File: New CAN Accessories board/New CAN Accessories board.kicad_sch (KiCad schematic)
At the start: 0 parts

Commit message: updated schematic to add high side sensing, haven't speced specific components yet
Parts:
- added C1, C2: 100nF, Capacitor_SMD:C_0805_2012Metric, symbol Device:C
- added D1, D2, D3, D4, D5, D6, D7, D9: LED, LED_SMD:LED_0805_2012Metric, symbol Device:LED
- added F1, F2, F3, F4, F5, F6, F7, F9: Fuse, FuseClips:3586KTR, symbol Device:Fuse
- added J1, J2, J3, J4, J5, J6, J7, J8: 39301040, Connector_Molex:Molex_Mini-Fit_Jr_5569-04A2_2x02_P4.20mm_Horizontal, symbol Connector_Generic:Conn_02x02_Top_Bottom
- added J10, J9: 39301060, Connector_Molex:Molex_Mini-Fit_Jr_5569-06A2_2x03_P4.20mm_Horizontal, symbol Connector_Generic:Conn_02x03_Top_Bottom
- added JP4: SolderJumper_2_Open, Jumper:SolderJumper-2_P1.3mm_Open_Pad1.0x1.5mm, symbol Jumper:SolderJumper_2_Open
- added Q1, Q2, Q3, Q4, Q5, Q6, Q7, Q8: IRF7455PBFTR, Package_SO:SOIC-8-1EP_3.9x4.9mm_P1.27mm_EP2.29x3mm, symbol Device:Q_NMOS_SGD
- added R1, R11, R13, R3, R42, R5, R7, R9: 100, Resistor_SMD:R_0805_2012Metric, symbol Device:R
- added R10, R12, R14, R2, R4, R43, R6, R8: 10K, Resistor_SMD:R_0805_2012Metric, symbol Device:R
- added R13: 120, Resistor_SMD:R_0805_2012Metric, symbol Device:R
- added R15, R16, R17, R18, R19, R20, R21, R22, R23, R24, R25, R26, R27, R28, R29, R30, R31, R32, R33, R34, R35, R36, R37, R38, R39, R40, R41, R44, R45, R46, R47, R48, R49, R50, R51, R52, R53, R54, R55, R56: R, symbol Device:R
- added U1: NUCLEO_L432KC, NUCLEO-L432KC:MODULE_NUCLEO-L432KC, symbol CAN_Accessories-rescue:NUCLEO_L432KC-NUCLEO-L432KC
- added U10, U3, U4, U5, U6, U7, U8, U9: OPA1662DGK, Package_SO:VSSOP-8_3x3mm_P0.65mm, symbol Amplifier_Operational:OPA1662DGK
- added U2: MCP2562FD-E_SN, MCP2562FD-E_SN:MCP2562FD-E_SN, symbol CAN_Accessories-rescue:MCP2562FD-E_SN-2021-02-19_16-08-03
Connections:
- new net: J1.1 (Pin_1), J1.2 (Pin_2), R17.2, R19.1
- new net: F1.1, J1.3 (Pin_3), J1.4 (Pin_4)
- new net: J2.1 (Pin_1), J2.2 (Pin_2), R22.2, R24.1
- new net: F2.1, J2.3 (Pin_3), J2.4 (Pin_4)
- new net: J3.1 (Pin_1), J3.2 (Pin_2), R27.2, R29.1
- new net: F3.1, J3.3 (Pin_3), J3.4 (Pin_4)
- new net: J4.1 (Pin_1), J4.2 (Pin_2), R32.2, R34.1
- new net: F4.1, J4.3 (Pin_3), J4.4 (Pin_4)
- new net: J5.1 (Pin_1), J5.2 (Pin_2), R36.2, R38.1
- new net: F5.1, J5.3 (Pin_3), J5.4 (Pin_4)
- new net: J7.1 (Pin_1), J7.2 (Pin_2), R48.2, R50.1
- new net: F6.1, J7.3 (Pin_3), J7.4 (Pin_4)
- new net: JP4.1 (A), R13.2
- new net: F1.2, Q1.3 (D)
- new net: D1.2 (A), R1.2
- new net: D5.2 (A), R9.2
- new net: R33.2, R35.1, U6.3 (+)
- new net: R23.2, R25.1, U4.3 (+)
- new net: R34.2, R40.1, U6.2 (-)
- new net: R50.2, R55.1, U9.2 (-)
- new net: R19.2, R20.1, U3.2 (-)
- new net: F7.1, J8.3 (Pin_3), J8.4 (Pin_4)
- new net: F7.2, Q8.3 (D)
- new net: R38.2, R41.1, U7.2 (-)
- new net: J6.2 (Pin_2), R44.2, R46.1
- new net: F4.2, Q4.3 (D)
- new net: J8.1 (Pin_1), J8.2 (Pin_2), R15.2, R52.1
- new net: R52.2, R56.1, U10.2 (-)
- new net: D2.2 (A), R3.2
- new net: R24.2, R26.1, U4.2 (-)
- new net: F9.1, J6.3 (Pin_3), J6.4 (Pin_4)
- new net: F9.2, Q6.3 (D)
- new net: R49.2, R51.1, U9.3 (+)
- new net: F6.2, Q7.3 (D)
- new net: R16.2, R53.1, U10.3 (+)
- new net: D7.2 (A), R13.2
- new net: F5.2, Q5.3 (D)
- new net: R45.2, R47.1, U8.3 (+)
- new net: F3.2, Q3.3 (D)
- new net: R46.2, R54.1, U8.2 (-)
- new net: R29.2, R31.1, U5.2 (-)
- new net: D9.2 (A), R42.2
- new net: D3.2 (A), R5.2
- new net: R37.2, R39.1, U7.3 (+)
- new net: R18.2, R21.1, U3.3 (+)
- new net: R28.2, R30.1, U5.3 (+)
- new net: D6.2 (A), R11.2
- new net: F2.2, Q2.3 (D)
- new net: D4.2 (A), R7.2
- new net +12V: J10.1 (Pin_1), J10.2 (Pin_2), J9.1 (Pin_1), J9.2 (Pin_2), R15.1, R16.1, R17.1, R18.1, R22.1, R23.1, R27.1, R28.1, R32.1, R33.1, R36.1, R37.1, R44.1, R45.1, R48.1, R49.1, U1.VIN
- new net 3V3: C2.1, U2.5 (VIO)
- new net 5V: C1.1, U1.5V, U2.3 (VDD)
- new net CANH: J10.5 (Pin_5), J9.5 (Pin_5), R13.1, U2.7 (CANH)
- new net CANL: J10.4 (Pin_4), J9.4 (Pin_4), JP4.2 (B), U2.6 (CANL)
- new net CANRX: U1.PA11 (D10), U2.4 (RXD)
- new net CANTX: U1.PA12 (D2), U2.1 (TXD)
- new net GATE1: Q1.2 (G), R1.1, R2.1, U1.PA2 (A7)
- new net GATE2: Q2.2 (G), R3.1, R4.1, U1.PA7 (A6)
- new net GATE3: Q3.2 (G), R5.1, R6.1, U1.PB7 (D4)
- new net GATE4: Q4.2 (G), R7.1, R8.1, U1.PB6 (D5)
- new net GATE5: Q5.2 (G), R10.1, R9.1, U1.PB5 (D11)
- new net GATE6: Q6.2 (G), Q7.2 (G), R11.1, R12.1, R42.1, R43.1, U1.PB4 (D12)
- new net GATE7: Q8.2 (G), R13.1, R14.1
- new net GND: C1.2, C2.2, D1.1 (K), D2.1 (K), D3.1 (K), D4.1 (K), D5.1 (K), D6.1 (K), D7.1 (K), D9.1 (K), J10.3 (Pin_3), J10.6 (Pin_6), J9.3 (Pin_3), J9.6 (Pin_6), Q1.1 (S), Q2.1 (S), Q3.1 (S), Q4.1 (S), Q5.1 (S), Q6.1 (S), Q7.1 (S), Q8.1 (S), R10.2, R12.2, R14.2, R2.2, R20.2, R26.2, R31.2, R4.2, R40.2, R41.2, R43.2, R54.2, R55.2, R56.2, R6.2, R8.2, U1.GND, U2.2 (VSS)
- new net OA1: R21.2, U1.PA0 (A0), U3.1
- new net OA2: R25.2, U1.PA1 (A1), U4.1
- new net OA3: R30.2, U1.PA3 (A2), U5.1
- new net OA4: R35.2, U1.PA4 (A3), U6.1
- new net OA5: R39.2, U1.PA5 (A4), U7.1
- new net OA6: R47.2, U1.PA6 (A5), U8.1
- new net OA7: R51.2, U1.PA8 (D9), U9.1
- new net OA8: R53.2, U1.PB1 (D6), U10.1
- new net STBY: U1.PA9 (D1), U2.8 (STBY)
- no-connect marks 0 -> 9

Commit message: updated kicad schematic to include new op amps and update layout
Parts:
- removed D4, D5, D6, D9: LED, LED_SMD:LED_0805_2012Metric, symbol Device:LED
- removed J4, J5, J6: 39301040, Connector_Molex:Molex_Mini-Fit_Jr_5569-04A2_2x02_P4.20mm_Horizontal, symbol Connector_Generic:Conn_02x02_Top_Bottom
- removed R10, R12, R14, R43: 10K, Resistor_SMD:R_0805_2012Metric, symbol Device:R
- removed R11, R42, R9: 100, Resistor_SMD:R_0805_2012Metric, symbol Device:R
- removed R15, R16, R21, R22, R25, R26, R27, R28, R29, R30, R31, R32, R33, R34, R35, R36, R37, R38, R39, R40, R41, R44, R45, R46, R47, R48, R49, R50, R51, R52, R53, R54, R55, R56: R, symbol Device:R
- removed U10, U3, U4, U5, U6, U7, U8, U9: OPA1662DGK, Package_SO:VSSOP-8_3x3mm_P0.65mm, symbol Amplifier_Operational:OPA1662DGK
- added D4 (x2), D5 (x2), D6 (x2), D8: LED, LED_SMD:LED_0805_2012Metric, symbol Device:LED
- added F10, F11, F8: Fuse, FuseClips:3586KTR, symbol Device:Fuse
- added J4 (x2), J5 (x2), J6 (x2): 39301040, Connector_Molex:Molex_Mini-Fit_Jr_5569-04A2_2x02_P4.20mm_Horizontal, symbol Connector_Generic:Conn_02x02_Top_Bottom
- added OP1, OP2, OP3, OP4, OP5, OP6, OP7, OP8, U6, U7, U8: MCP6C02T-020E/CHY, SOT-23-6_CHY_MCH, symbol sym:MCP6C02T-020E_CHY
- added Q10, Q11, Q9: IRF7455PBFTR, Package_SO:SOIC-8-1EP_3.9x4.9mm_P1.27mm_EP2.29x3mm, symbol Device:Q_NMOS_SGD
- added R10 (x2), R12, R14 (x2), R16, R21: 10K, Resistor_SMD:R_0805_2012Metric, symbol Device:R
- added R11, R12, R15, R16, R9 (x2): 100, Resistor_SMD:R_0805_2012Metric, symbol Device:R
- added R11, R15, R21, R22 (x2): 0.05, symbol Device:R
- added R57: 10K, symbol Device:R
- added SW1: SW_SPST, symbol Switch:SW_SPST
- R17, R18, R19, R20, R23, R24: value R -> 0.05
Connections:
- net GATE7 is gone; now on net GATE1: Q8.2 (G), R13.1
- net +12V: now also R19.1, R20.1, R24.1, OP1.3 (VIP), OP2.3 (VIP), OP3.3 (VIP), OP4.3 (VIP), OP5.3 (VIP), OP6.3 (VIP), OP7.3 (VIP), OP8.3 (VIP), R11.1, R15.1, R21.1, R22.1, R22.1, U6.3 (VIP), U7.3 (VIP), U8.3 (VIP)
- net 5V: now also OP1.6 (VDD), OP2.6 (VDD), OP3.6 (VDD), OP4.6 (VDD), OP5.6 (VDD), OP6.6 (VDD), OP7.6 (VDD), OP8.6 (VDD), U6.6 (VDD), U7.6 (VDD), U8.6 (VDD)
- net GATE1: now also Q2.2 (G), Q3.2 (G), Q4.2 (G), Q5.2 (G), Q6.2 (G), Q7.2 (G), R3.1, R4.1, R5.1, R6.1, R7.1, R8.1, U1.PB1 (D6), Q10.2 (G), Q11.2 (G), Q9.2 (G), R10.1, R10.1, R11.1, R12.1, R12.1, R14.1, R14.1, R15.1, R16.1, R16.1, R21.1, R9.1, R9.1; no longer U1.PA2 (A7)
- net GATE2: now also U1.PA8 (D9); no longer Q2.2 (G), R3.1, R4.1, U1.PA7 (A6)
- net GATE3: no longer Q3.2 (G), R5.1, R6.1
- net GATE4: no longer Q4.2 (G), R7.1, R8.1
- net GATE5: no longer Q5.2 (G)
- net GATE6: no longer Q6.2 (G), Q7.2 (G)
- net GND: now also D4.1 (K), D5.1 (K), D6.1 (K), D8.1 (K), OP1.2 (VSS), OP1.5 (VREF), OP2.2 (VSS), OP2.5 (VREF), OP3.2 (VSS), OP3.5 (VREF), OP4.2 (VSS), OP4.5 (VREF), OP5.2 (VSS), OP5.5 (VREF), OP6.2 (VSS), OP6.5 (VREF), OP7.2 (VSS), OP7.5 (VREF), OP8.2 (VSS), OP8.5 (VREF), Q10.1 (S), Q11.1 (S), Q9.1 (S), R10.2, R12.2, R14.2, R16.2, R57.2, U6.2 (VSS), U7.2 (VSS), U8.2 (VSS); no longer Q4.1 (S), Q5.1 (S), Q6.1 (S), R20.2
- net OA1: now also OP1.1 (VOUT), U6.1 (VOUT), U7.1 (VOUT), U8.1 (VOUT)
- net OA2: now also OP2.1 (VOUT)
- net OA3: now also OP3.1 (VOUT)
- net OA4: now also OP4.1 (VOUT)
- net OA5: now also OP5.1 (VOUT)
- net OA6: now also OP6.1 (VOUT)
- net OA7: now also U1.PA7 (A6), OP7.1 (VOUT); no longer U1.PA8 (D9)
- net OA8: now also U1.PA2 (A7), OP8.1 (VOUT); no longer U1.PB1 (D6)
- net at J1.1 (Pin_1), J1.2 (Pin_2), R17.2: now also OP1.4 (VIM); no longer R19.1
- net at J2.1 (Pin_1), J2.2 (Pin_2): now also R18.2, OP2.4 (VIM); no longer R24.1
- net at J2.3 (Pin_3), J2.4 (Pin_4): now also F8.1; no longer F2.1
- net at J3.1 (Pin_1), J3.2 (Pin_2): now also R19.2, OP3.4 (VIM)
- net at J3.3 (Pin_3), J3.4 (Pin_4): now also F2.1; no longer F3.1
- net at F4.1: now also J4.3 (Pin_3), J4.4 (Pin_4)
- net at F5.1: now also J5.3 (Pin_3), J5.4 (Pin_4)
- net at J7.1 (Pin_1), J7.2 (Pin_2): now also R23.2, OP7.4 (VIM)
- net at J7.3 (Pin_3), J7.4 (Pin_4): now also F10.1; no longer F6.1
- net at U1.3V3: now also SW1.1 (A)
- net at U1.PB3 (D13): now also R57.1, SW1.2 (B)
- net at J8.3 (Pin_3), J8.4 (Pin_4): now also F11.1; no longer F7.1
- net at Q8.3 (D): now also F9.2; no longer F7.2
- net at J8.1 (Pin_1), J8.2 (Pin_2): now also R24.2, OP8.4 (VIM)
- net at F9.1: now also J6.3 (Pin_3), J6.4 (Pin_4)
- net at Q6.3 (D): now also F6.2; no longer F9.2
- net at Q7.3 (D): now also F7.2; no longer F6.2
- net at R7.2: now also D4.2 (A)
- new net: J4.1 (Pin_1), J4.2 (Pin_2), R11.2, U6.4 (VIM)
- new net: D4.1 (K), Q4.1 (S), R10.2, U6.5 (VREF)
- new net: J6.1 (Pin_1), J6.2 (Pin_2), OP6.4 (VIM), R22.2
- new net: J4.1 (Pin_1), J4.2 (Pin_2), OP4.4 (VIM), R20.2
- new net: F6.1, J6.3 (Pin_3), J6.4 (Pin_4)
- new net: J6.1 (Pin_1), J6.2 (Pin_2), R22.2, U8.4 (VIM)
- new net: D6.1 (K), Q6.1 (S), R21.2, U8.5 (VREF)
- new net: J5.1 (Pin_1), J5.2 (Pin_2), OP5.4 (VIM), R21.2
- new net: D4.2 (A), R9.2
- new net: D6.2 (A), R11.2
- new net: D5.1 (K), Q5.1 (S), R14.2, U7.5 (VREF)
- new net: F3.1, J4.3 (Pin_3), J4.4 (Pin_4)
- new net: D5.2 (A), R12.2
- new net: F11.2, Q11.3 (D)
- new net: F10.2, Q10.3 (D)
- new net: F8.2, Q9.3 (D)
- new net: F7.1, J5.3 (Pin_3), J5.4 (Pin_4)
- new net: D8.2 (A), R15.2
- new net: J5.1 (Pin_1), J5.2 (Pin_2), R15.2, U7.4 (VIM)
- new net: D6.2 (A), R16.2
- new net: D5.2 (A), R9.2
- no-connect marks 9 -> 7
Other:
- moved on the sheet: C1, C2, D1, F1, J1, J10, J9, JP4, Q1, R1, R13, R17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

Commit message: updated schematic again, all parts match bom, for final review
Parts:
- removed Q1, Q10, Q11, Q2, Q3, Q7, Q8, Q9: IRF7455PBFTR, Package_SO:SOIC-8-1EP_3.9x4.9mm_P1.27mm_EP2.29x3mm, symbol Device:Q_NMOS_SGD
- removed SW1: SW_SPST, symbol Switch:SW_SPST
- added Q1, Q2, Q4, Q5, Q6, Q7, Q8: IRLML6344TRPBF, IRLML6344TRPBF:TRANS_IRLML6344TRPBF, symbol sym:IRLML6344TRPBF
- added R27: 10K, symbol Device:R
- added SW1, SW2: JS202011CQN, SWITCH_011CQN, symbol sym:JS202011CQN
- renumbered F8 to F2, F2 to F3, F3 to F4, F7 to F5, F9 to F6, F10 to F7, R13 to R25, R57 to R26
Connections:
- net 3V3: now also SW1.1, SW1.2, SW1.3, SW2.1, SW2.2, SW2.3
- net GATE1: now also Q1.1; no longer R10.1, R11.1, R12.1, R13.1, R14.1, R15.1, R16.1, R3.1, R4.1, R5.1, R6.1, R7.1, R8.1, R9.1
- net GATE2: now also R3.1, R4.1, Q2.1
- net GATE3: now also R5.1, R6.1, Q1.1
- net GATE4: now also R7.1, R8.1, Q4.1
- net GATE5: now also R10.1, R9.1, Q5.1
- net GATE6: now also R11.1, R12.1, Q6.1
- net GND: now also Q1.2, Q2.2, Q4.2, Q5.2, Q6.2, Q7.2, Q8.2, R27.2
- net at F1.2: now also Q1.3
- net BOARD_SW: now reaches U1.PB0 (D3)
- net BOARD_SW: now also R27.1, SW2.4, SW2.5, SW2.6
- net TELEM_SW: now reaches R26.1, U1.PB3 (D13)
- net TELEM_SW: now also SW1.4, SW1.5, SW1.6
- net at F6.2: now also Q6.3
- net at F4.2: now also Q4.3
- net at F11.2: now also Q8.3
- net at F7.2: now also Q7.3
- net at F3.2: now also Q1.3
- net at F2.2: now also Q2.3
- net at F5.2: now also Q5.3
- new net GATE7: Q7.1, R13.1, R14.1
- new net GATE8: Q8.1, R15.1, R16.1
- no-connect marks 7 -> 6
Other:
- moved on the sheet: C1, C2, F1, F11, F2, F3, F4, F5, F6, F7, J10, J9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

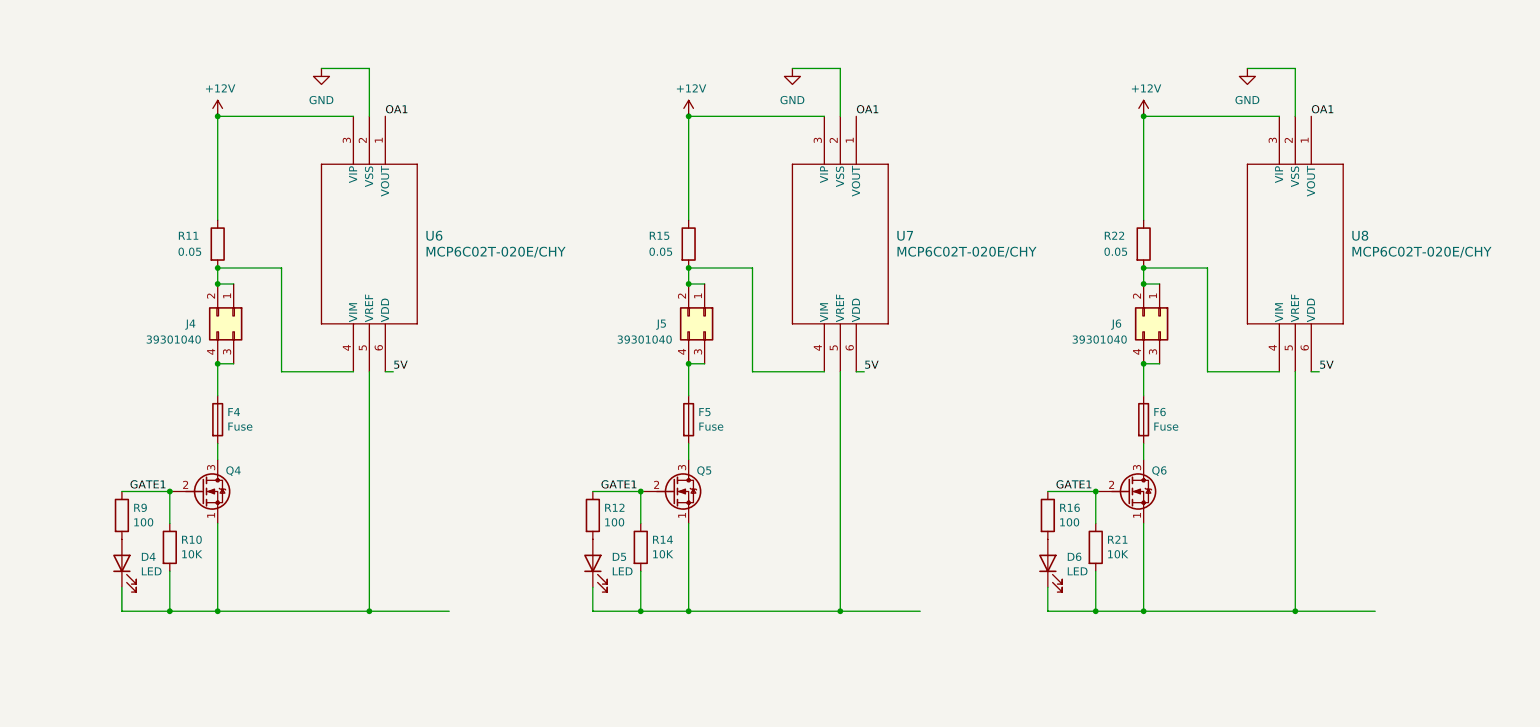
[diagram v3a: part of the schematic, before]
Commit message: deleted 3 outside connectors
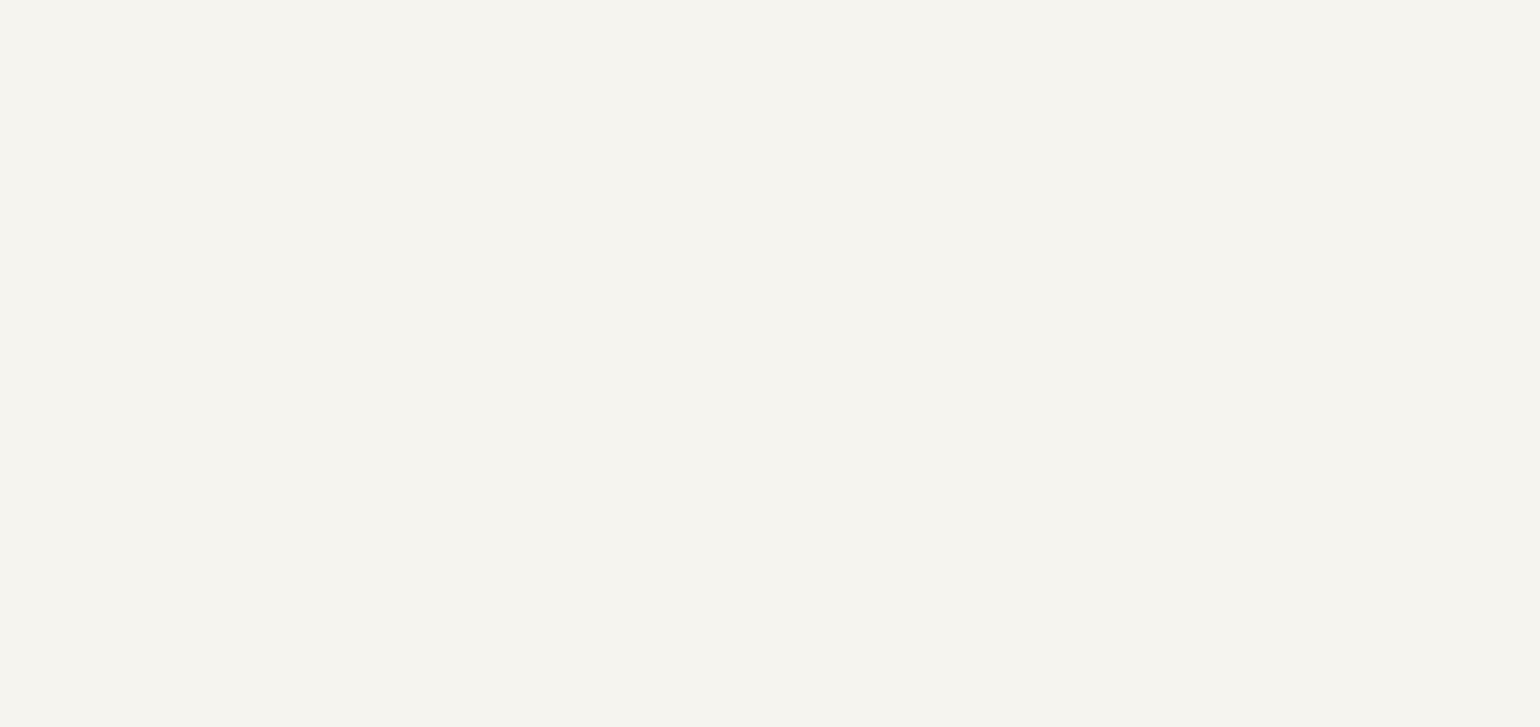
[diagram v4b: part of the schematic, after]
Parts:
- removed D4, D5, D6: LED, LED_SMD:LED_0805_2012Metric, symbol Device:LED
- removed F4, F5, F6: Fuse, FuseClips:3586KTR, symbol Device:Fuse
- removed J4, J5, J6: 39301040, Connector_Molex:Molex_Mini-Fit_Jr_5569-04A2_2x02_P4.20mm_Horizontal, symbol Connector_Generic:Conn_02x02_Top_Bottom
- removed Q4, Q5, Q6: IRF7455PBFTR, Package_SO:SOIC-8-1EP_3.9x4.9mm_P1.27mm_EP2.29x3mm, symbol Device:Q_NMOS_SGD
- removed R10, R14, R21: 10K, Resistor_SMD:R_0805_2012Metric, symbol Device:R
- removed R11, R15, R22: 0.05, symbol Device:R
- removed R12, R16, R9: 100, Resistor_SMD:R_0805_2012Metric, symbol Device:R
- removed U6, U7, U8: MCP6C02T-020E/CHY, SOT-23-6_CHY_MCH, symbol sym:MCP6C02T-020E_CHY
- added Q1: IRLML6344TRPBF, IRLML6344TRPBF:TRANS_IRLML6344TRPBF, symbol sym:IRLML6344TRPBF
- renumbered Q1 to Q3
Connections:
- net GATE1: now also Q1.1; no longer Q3.1
- net GND: now also Q1.2
- net at F1.2: now also Q1.3; no longer Q3.3

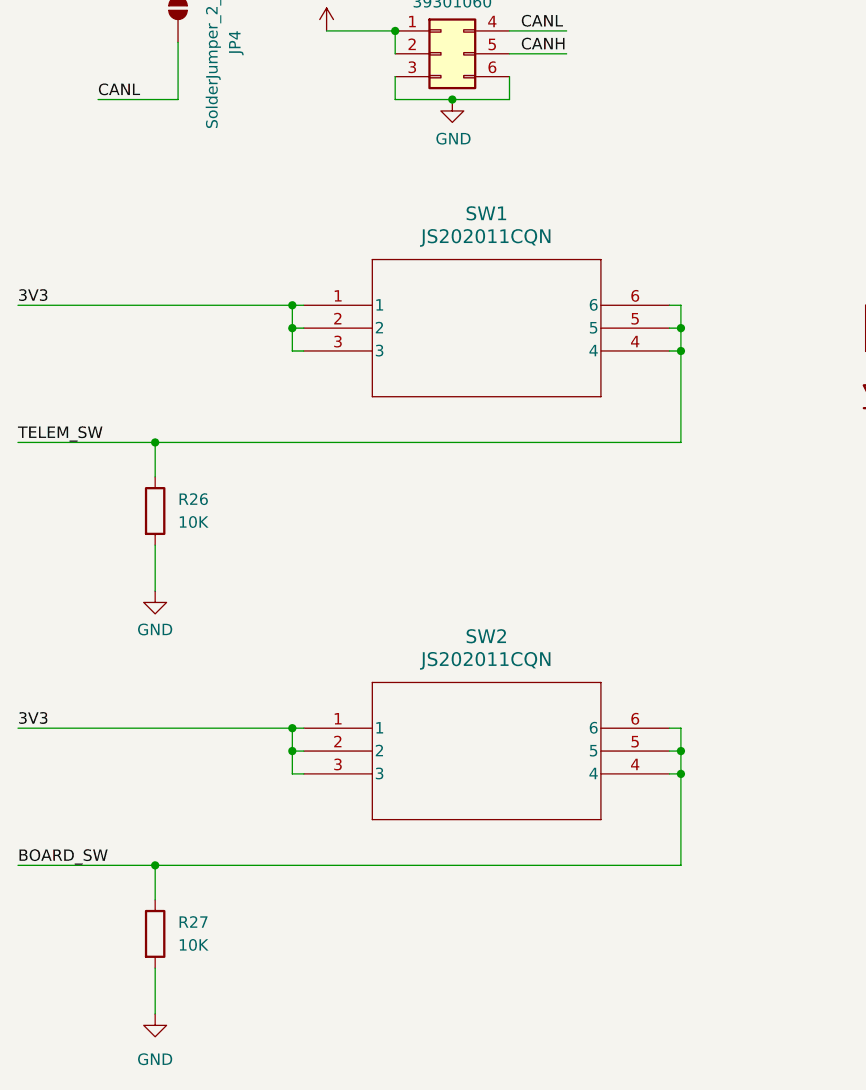
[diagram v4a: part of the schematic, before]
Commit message: Changed switch symbols
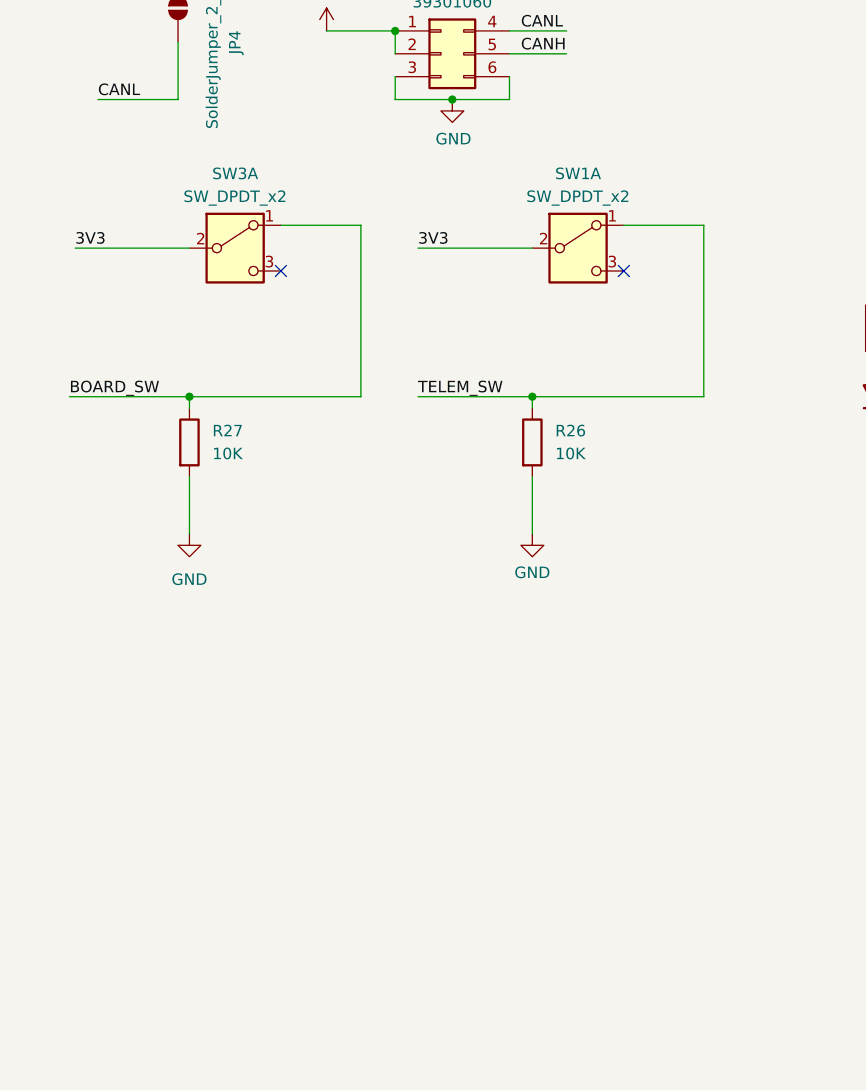
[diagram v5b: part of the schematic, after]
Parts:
- removed SW1, SW2: JS202011CQN, SWITCH_011CQN, symbol sym:JS202011CQN
- added SW1, SW3: SW_DPDT_x2, symbol Switch:SW_DPDT_x2
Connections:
- net 3V3: now also SW1.2 (B), SW3.2 (B)
- net BOARD_SW: now also SW3.1 (A)
- net TELEM_SW: now also SW1.1 (A)
- no-connect marks 6 -> 8
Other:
- moved on the sheet: R26, R27

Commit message: Footprints updated
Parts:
- F1, F11, F2, F3, F4, F5, F6, F7: footprint FuseClips:3586KTR -> footprint:3586KTR
- OP1, OP2, OP3, OP4, OP5, OP6, OP7, OP8: footprint SOT-23-6_CHY_MCH -> footprint:SOT-23-6_CHY_MCH-M
- Q1, Q2, Q3, Q4, Q5, Q6, Q7, Q8: footprint IRLML6344TRPBF:TRANS_IRLML6344TRPBF -> footprint:TRANS_IRLML6344TRPBF
- R17, R18, R19, R20, R21, R22, R23, R24: footprint (none) -> Resistor_SMD:R_2512_6332Metric_Pad1.40x3.35mm_HandSolder
- R26, R27: footprint (none) -> Resistor_SMD:R_0805_2012Metric
- SW1, SW3: footprint (none) -> footprint:SWITCH_011CQN
- U1: footprint NUCLEO-L432KC:MODULE_NUCLEO-L432KC -> footprint:MODULE_NUCLEO-L432KC
- U2: footprint MCP2562FD-E_SN:MCP2562FD-E_SN -> footprint:MCP2562FD-E_SN
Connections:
- net 3V3: now also U1.3V3
